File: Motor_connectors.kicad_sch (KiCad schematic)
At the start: 0 parts

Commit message: Motor connectors added check pinout with motor wiring
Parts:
- added UR1, UR2, UR3: 2367196-8, symbol 2367196-8:2367196-8
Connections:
- new net GND: UR1.4, UR1.MP1, UR1.MP2, UR2.4, UR2.MP1, UR2.MP2, UR3.4, UR3.MP1, UR3.MP2
- new net MOT_POW: UR1.5, UR2.5, UR3.5
- new net U_1: UR1.3
- new net U_2: UR2.3
- new net U_3: UR3.3
- new net U_HP_1: UR1.8
- new net U_HP_2: UR2.8
- new net U_HP_3: UR3.8
- new net V_1: UR1.2
- new net V_2: UR2.2
- new net V_3: UR3.2
- new net V_HP_1: UR1.7
- new net V_HP_2: UR2.7
- new net V_HP_3: UR3.7
- new net W_1: UR1.1
- new net W_2: UR2.1
- new net W_3: UR3.1
- new net W_HP_1: UR1.6
- new net W_HP_2: UR2.6
- new net W_HP_3: UR3.6

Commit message: MCU interfaces are done! Check the Changes and Complete ERC modifications
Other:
- company: (none) -> Parikshit Student Satellite Team
- title: (none) -> AOCS BOARD
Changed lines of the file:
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@@
 (kicad_sch (version 20211123) (generator eeschema)
   (paper "A4")
+  (title_block
+    (title "AOCS BOARD")
+    (company "Parikshit Student Satellite Team")
+  )
   (junction (at 133.35 55.88) (diameter 0) (color 0 0 0 0)
   )
@@
   )
   (wire (pts (xy 66.04 121.92) (xy 69.85 121.92))
+    (stroke (width 0) (type default) (color 0 0 0 0))
+  )
+  (wire (pts (xy 26.67 167.64) (xy 26.67 166.37))
     (stroke (width 0) (type default) (color 0 0 0 0))
   )
@@
   (symbol (lib_id "power:GND") (at 85.09 60.96 0) (unit 1)
     (in_bom yes) (on_board yes) (fields_autoplaced)
-    (property "Reference" "#PWR?" (id 0) (at 85.09 67.31 0)
+    (property "Reference" "#PWR0242" (id 0) (at 85.09 67.31 0)
       (effects (font (size 1.27 1.27)) hide)
     )
@@
   (symbol (lib_id "power:GND") (at 181.61 60.96 0) (unit 1)
     (in_bom yes) (on_board yes) (fields_autoplaced)
-    (property "Reference" "#PWR?" (id 0) (at 181.61 67.31 0)
+    (property "Reference" "#PWR0244" (id 0) (at 181.61 67.31 0)
       (effects (font (size 1.27 1.27)) hide)
     )
@@
   (symbol (lib_id "power:GND") (at 86.36 116.84 0) (unit 1)
     (in_bom yes) (on_board yes) (fields_autoplaced)
-    (property "Reference" "#PWR?" (id 0) (at 86.36 123.19 0)
+    (property "Reference" "#PWR0240" (id 0) (at 86.36 123.19 0)
       (effects (font (size 1.27 1.27)) hide)
     )
@@
   (symbol (lib_id "power:GND") (at 35.56 57.15 0) (unit 1)
     (in_bom yes) (on_board yes) (fields_autoplaced)
-    (property "Reference" "#PWR?" (id 0) (at 35.56 63.5 0)
+    (property "Reference" "#PWR0239" (id 0) (at 35.56 63.5 0)
       (effects (font (size 1.27 1.27)) hide)
     )
@@
     )
     (property "Datasheet" "" (id 3) (at 35.56 57.15 0)
+      (effects (font (size 1.27 1.27)) hide)
+    )
+    (pin "1")
+  )
+  (symbol (lib_id "power:GND") (at 26.67 167.64 0) (unit 1)
+    (in_bom yes) (on_board yes) (fields_autoplaced)
+    (property "Reference" "#PWR0275" (id 0) (at 26.67 173.99 0)
+      (effects (font (size 1.27 1.27)) hide)
+    )
+    (property "Value" "GND" (id 1) (at 26.67 172.085 0))
+    (property "Footprint" "" (id 2) (at 26.67 167.64 0)
+      (effects (font (size 1.27 1.27)) hide)
+    )
+    (property "Datasheet" "" (id 3) (at 26.67 167.64 0)
       (effects (font (size 1.27 1.27)) hide)
     )
@@
   (symbol (lib_id "power:GND") (at 38.1 114.3 0) (unit 1)
     (in_bom yes) (on_board yes) (fields_autoplaced)
-    (property "Reference" "#PWR?" (id 0) (at 38.1 120.65 0)
+    (property "Reference" "#PWR0241" (id 0) (at 38.1 120.65 0)
       (effects (font (size 1.27 1.27)) hide)
     )
@@
   (symbol (lib_id "power:GND") (at 133.35 58.42 0) (unit 1)
     (in_bom yes) (on_board yes) (fields_autoplaced)
-    (property "Reference" "#PWR?" (id 0) (at 133.35 64.77 0)
+    (property "Reference" "#PWR0243" (id 0) (at 133.35 64.77 0)
       (effects (font (size 1.27 1.27)) hide)
     )
@@
       (effects (font (size 1.27 1.27)) hide)
     )
+    (pin "1")
+  )
+  (symbol (lib_id "power:PWR_FLAG") (at 26.67 166.37 0) (unit 1)
+    (in_bom yes) (on_board yes) (fields_autoplaced)
+    (property "Reference" "#FLG0111" (id 0) (at 26.67 164.465 0)
+      (effects (font (size 1.27 1.27)) hide)
+    )
+    (property "Value" "PWR_FLAG" (id 1) (at 26.67 160.655 0))
+    (property "Footprint" "" (id 2) (at 26.67 166.37 0)
+      (effects (font (size 1.27 1.27)) hide)
+    )
+    (property "Datasheet" "~" (id 3) (at 26.67 166.37 0)
+      (effects (font (size 1.27 1.27)) hide)
+    )

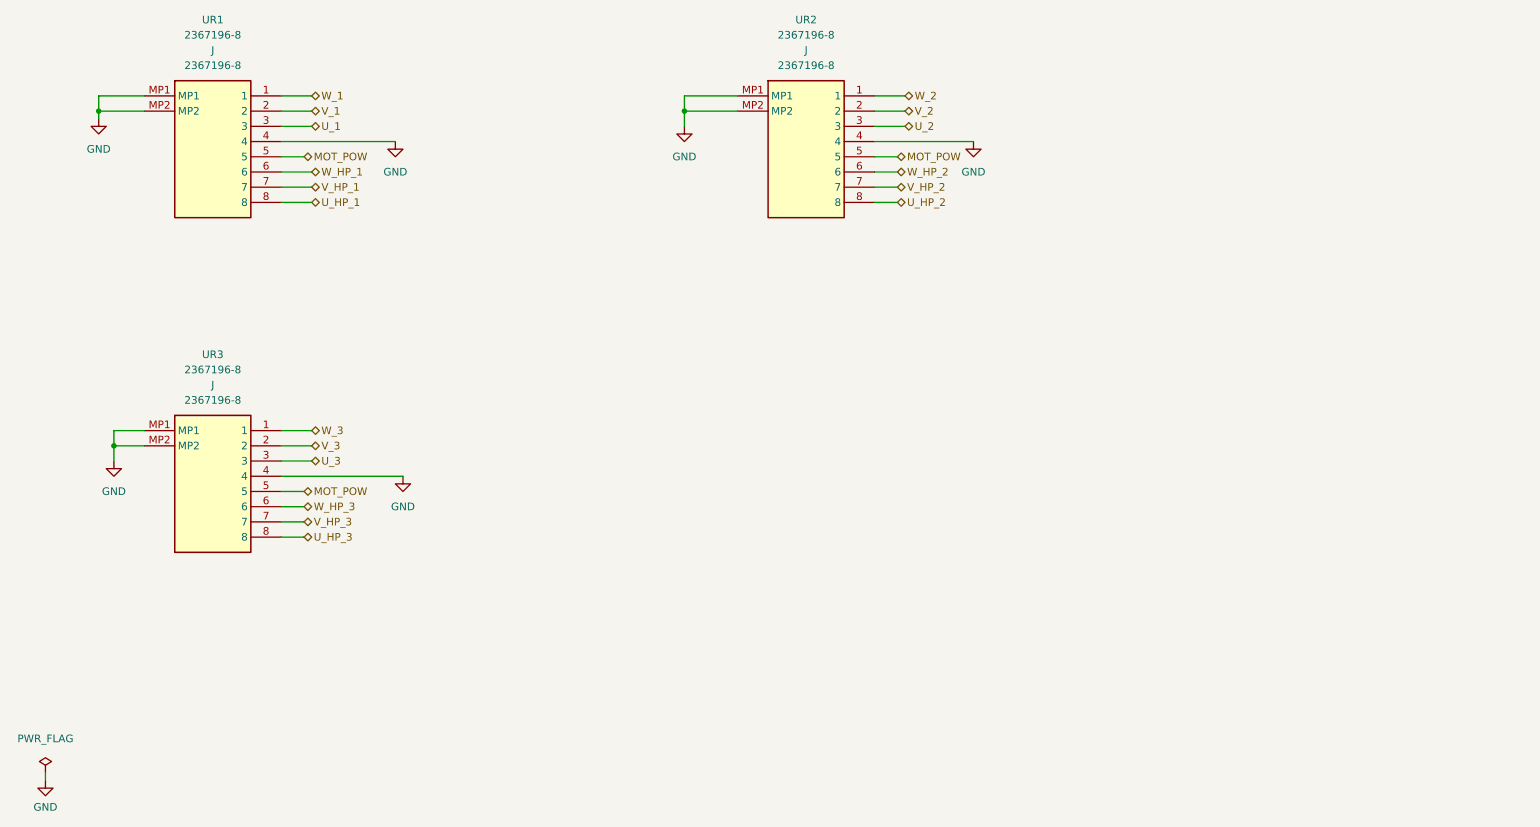
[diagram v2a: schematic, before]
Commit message: Max ERC errors corrected
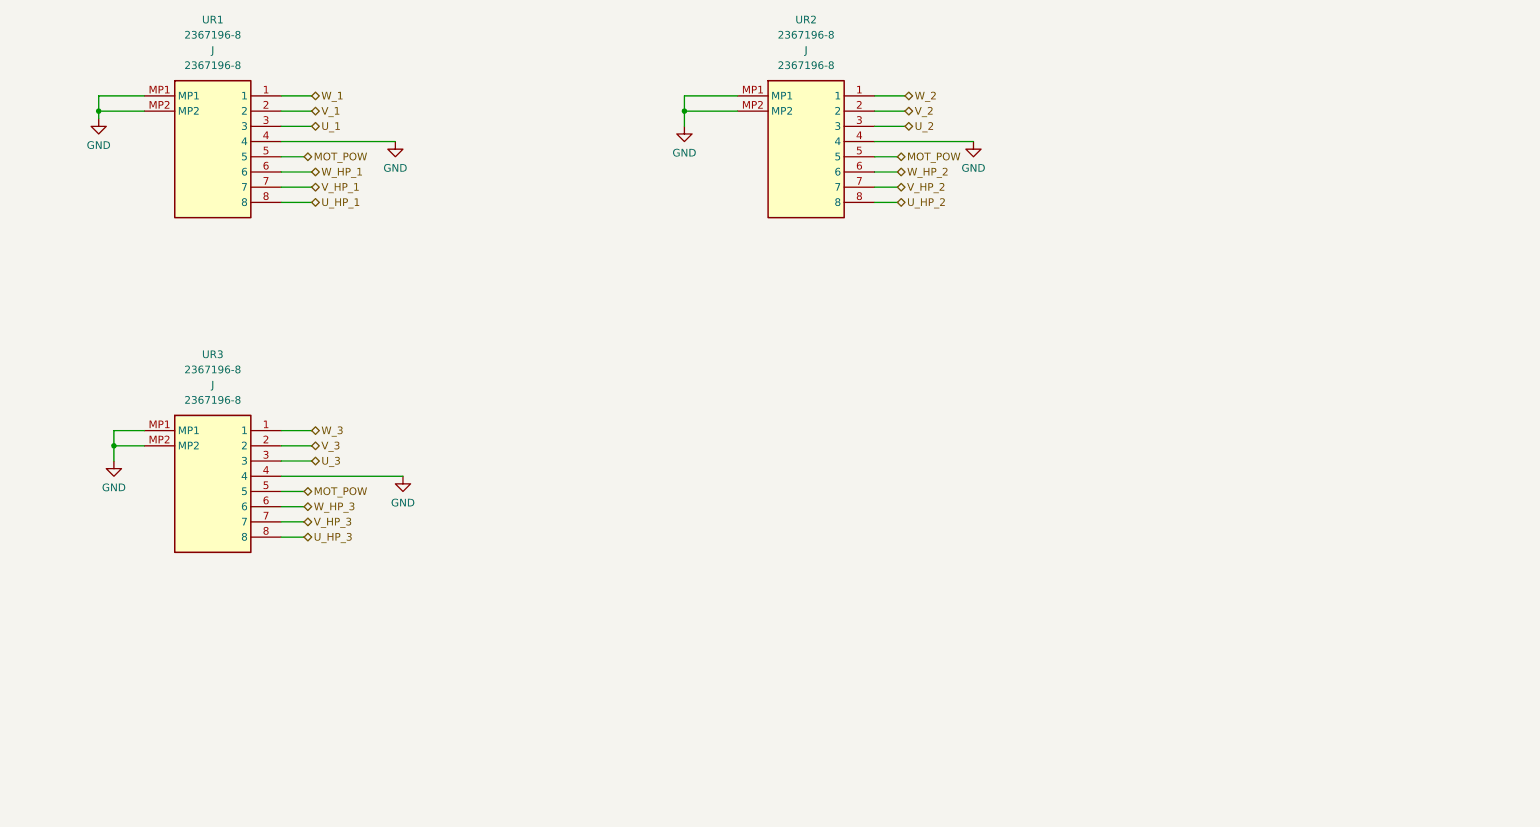
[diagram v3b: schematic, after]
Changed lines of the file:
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@@
-    (stroke (width 0) (type default) (color 0 0 0 0))
-  )
-  (wire (pts (xy 26.67 167.64) (xy 26.67 166.37))
     (stroke (width 0) (type default) (color 0 0 0 0))
   )
@@
     (pin "MP2")
   )
-  (symbol (lib_id "power:GND") (at 85.09 60.96 0) (unit 1)
-    (in_bom yes) (on_board yes) (fields_autoplaced)
-    (property "Reference" "#PWR0242" (id 0) (at 85.09 67.31 0)
-      (effects (font (size 1.27 1.27)) hide)
-    )
-    (property "Value" "GND" (id 1) (at 85.09 66.04 0))
-    (property "Footprint" "" (id 2) (at 85.09 60.96 0)
-      (effects (font (size 1.27 1.27)) hide)
-    )
-    (property "Datasheet" "" (id 3) (at 85.09 60.96 0)
-      (effects (font (size 1.27 1.27)) hide)
-    )
-    (pin "1")
-  )
-  (symbol (lib_id "power:GND") (at 181.61 60.96 0) (unit 1)
+  (symbol (lib_id "upsat-comms-hardware:GND") (at 133.35 58.42 0) (unit 1)
+    (in_bom yes) (on_board yes) (fields_autoplaced)
+    (property "Reference" "#PWR0243" (id 0) (at 133.35 64.77 0)
+      (effects (font (size 1.27 1.27)) hide)
+    )
+    (property "Value" "GND" (id 1) (at 133.35 62.865 0))
+    (property "Footprint" "" (id 2) (at 133.35 58.42 0))
+    (property "Datasheet" "" (id 3) (at 133.35 58.42 0))
+    (pin "1")
+  )
+  (symbol (lib_id "upsat-comms-hardware:GND") (at 85.09 60.96 0) (unit 1)
+    (in_bom yes) (on_board yes) (fields_autoplaced)
+    (property "Reference" "#PWR0239" (id 0) (at 85.09 67.31 0)
+      (effects (font (size 1.27 1.27)) hide)
+    )
+    (property "Value" "GND" (id 1) (at 85.09 65.405 0))
+    (property "Footprint" "" (id 2) (at 85.09 60.96 0))
+    (property "Datasheet" "" (id 3) (at 85.09 60.96 0))
+    (pin "1")
+  )
+  (symbol (lib_id "upsat-comms-hardware:GND") (at 181.61 60.96 0) (unit 1)
     (in_bom yes) (on_board yes) (fields_autoplaced)
     (property "Reference" "#PWR0244" (id 0) (at 181.61 67.31 0)
       (effects (font (size 1.27 1.27)) hide)
     )
-    (property "Value" "GND" (id 1) (at 181.61 66.04 0))
-    (property "Footprint" "" (id 2) (at 181.61 60.96 0)
-      (effects (font (size 1.27 1.27)) hide)
-    )
-    (property "Datasheet" "" (id 3) (at 181.61 60.96 0)
-      (effects (font (size 1.27 1.27)) hide)
-    )
-    (pin "1")
-  )
-  (symbol (lib_id "power:GND") (at 86.36 116.84 0) (unit 1)
-    (in_bom yes) (on_board yes) (fields_autoplaced)
-    (property "Reference" "#PWR0240" (id 0) (at 86.36 123.19 0)
-      (effects (font (size 1.27 1.27)) hide)
-    )
-    (property "Value" "GND" (id 1) (at 86.36 121.92 0))
-    (property "Footprint" "" (id 2) (at 86.36 116.84 0)
-      (effects (font (size 1.27 1.27)) hide)
-    )
-    (property "Datasheet" "" (id 3) (at 86.36 116.84 0)
-      (effects (font (size 1.27 1.27)) hide)
-    )
-    (pin "1")
-  )
-  (symbol (lib_id "power:GND") (at 35.56 57.15 0) (unit 1)
-    (in_bom yes) (on_board yes) (fields_autoplaced)
-    (property "Reference" "#PWR0239" (id 0) (at 35.56 63.5 0)
-      (effects (font (size 1.27 1.27)) hide)
-    )
-    (property "Value" "GND" (id 1) (at 35.56 62.23 0))
-    (property "Footprint" "" (id 2) (at 35.56 57.15 0)
-      (effects (font (size 1.27 1.27)) hide)
-    )
-    (property "Datasheet" "" (id 3) (at 35.56 57.15 0)
-      (effects (font (size 1.27 1.27)) hide)
-    )
-    (pin "1")
-  )
-  (symbol (lib_id "power:GND") (at 26.67 167.64 0) (unit 1)
-    (in_bom yes) (on_board yes) (fields_autoplaced)
-    (property "Reference" "#PWR0275" (id 0) (at 26.67 173.99 0)
-      (effects (font (size 1.27 1.27)) hide)
-    )
-    (property "Value" "GND" (id 1) (at 26.67 172.085 0))
-    (property "Footprint" "" (id 2) (at 26.67 167.64 0)
-      (effects (font (size 1.27 1.27)) hide)
-    )
-    (property "Datasheet" "" (id 3) (at 26.67 167.64 0)
-      (effects (font (size 1.27 1.27)) hide)
-    )
+    (property "Value" "GND" (id 1) (at 181.61 65.405 0))
+    (property "Footprint" "" (id 2) (at 181.61 60.96 0))
+    (property "Datasheet" "" (id 3) (at 181.61 60.96 0))
+    (pin "1")
+  )
+  (symbol (lib_id "upsat-comms-hardware:GND") (at 35.56 57.15 0) (unit 1)
+    (in_bom yes) (on_board yes) (fields_autoplaced)
+    (property "Reference" "#PWR0240" (id 0) (at 35.56 63.5 0)
+      (effects (font (size 1.27 1.27)) hide)
+    )
+    (property "Value" "GND" (id 1) (at 35.56 61.595 0))
+    (property "Footprint" "" (id 2) (at 35.56 57.15 0))
+    (property "Datasheet" "" (id 3) (at 35.56 57.15 0))
     (pin "1")
   )
@@
     (pin "MP2")
   )
-  (symbol (lib_id "power:GND") (at 38.1 114.3 0) (unit 1)
-    (in_bom yes) (on_board yes) (fields_autoplaced)
-    (property "Reference" "#PWR0241" (id 0) (at 38.1 120.65 0)
-      (effects (font (size 1.27 1.27)) hide)
-    )
-    (property "Value" "GND" (id 1) (at 38.1 119.38 0))
-    (property "Footprint" "" (id 2) (at 38.1 114.3 0)
-      (effects (font (size 1.27 1.27)) hide)
-    )
-    (property "Datasheet" "" (id 3) (at 38.1 114.3 0)
-      (effects (font (size 1.27 1.27)) hide)
-    )
-    (pin "1")
-  )
-  (symbol (lib_id "power:GND") (at 133.35 58.42 0) (unit 1)
-    (in_bom yes) (on_board yes) (fields_autoplaced)
-    (property "Reference" "#PWR0243" (id 0) (at 133.35 64.77 0)
-      (effects (font (size 1.27 1.27)) hide)
-    )
-    (property "Value" "GND" (id 1) (at 133.35 63.5 0))
-    (property "Footprint" "" (id 2) (at 133.35 58.42 0)
-      (effects (font (size 1.27 1.27)) hide)
-    )
-    (property "Datasheet" "" (id 3) (at 133.35 58.42 0)
-      (effects (font (size 1.27 1.27)) hide)
-    )
-    (pin "1")
-  )
-  (symbol (lib_id "power:PWR_FLAG") (at 26.67 166.37 0) (unit 1)
-    (in_bom yes) (on_board yes) (fields_autoplaced)
-    (property "Reference" "#FLG0111" (id 0) (at 26.67 164.465 0)
-      (effects (font (size 1.27 1.27)) hide)
-    )
-    (property "Value" "PWR_FLAG" (id 1) (at 26.67 160.655 0))
-    (property "Footprint" "" (id 2) (at 26.67 166.37 0)
-      (effects (font (size 1.27 1.27)) hide)
-    )
-    (property "Datasheet" "~" (id 3) (at 26.67 166.37 0)
-      (effects (font (size 1.27 1.27)) hide)
-    )
+  (symbol (lib_id "upsat-comms-hardware:GND") (at 86.36 116.84 0) (unit 1)
+    (in_bom yes) (on_board yes) (fields_autoplaced)
+    (property "Reference" "#PWR0241" (id 0) (at 86.36 123.19 0)
+      (effects (font (size 1.27 1.27)) hide)
+    )
+    (property "Value" "GND" (id 1) (at 86.36 121.285 0))
+    (property "Footprint" "" (id 2) (at 86.36 116.84 0))
+    (property "Datasheet" "" (id 3) (at 86.36 116.84 0))
     (pin "1")
   )
@@
     (pin "MP2")
   )
+  (symbol (lib_id "upsat-comms-hardware:GND") (at 38.1 114.3 0) (unit 1)
+    (in_bom yes) (on_board yes) (fields_autoplaced)
+    (property "Reference" "#PWR0242" (id 0) (at 38.1 120.65 0)
+      (effects (font (size 1.27 1.27)) hide)
+    )
+    (property "Value" "GND" (id 1) (at 38.1 118.745 0))
+    (property "Footprint" "" (id 2) (at 38.1 114.3 0))
+    (property "Datasheet" "" (id 3) (at 38.1 114.3 0))
+    (pin "1")
+  )
 )

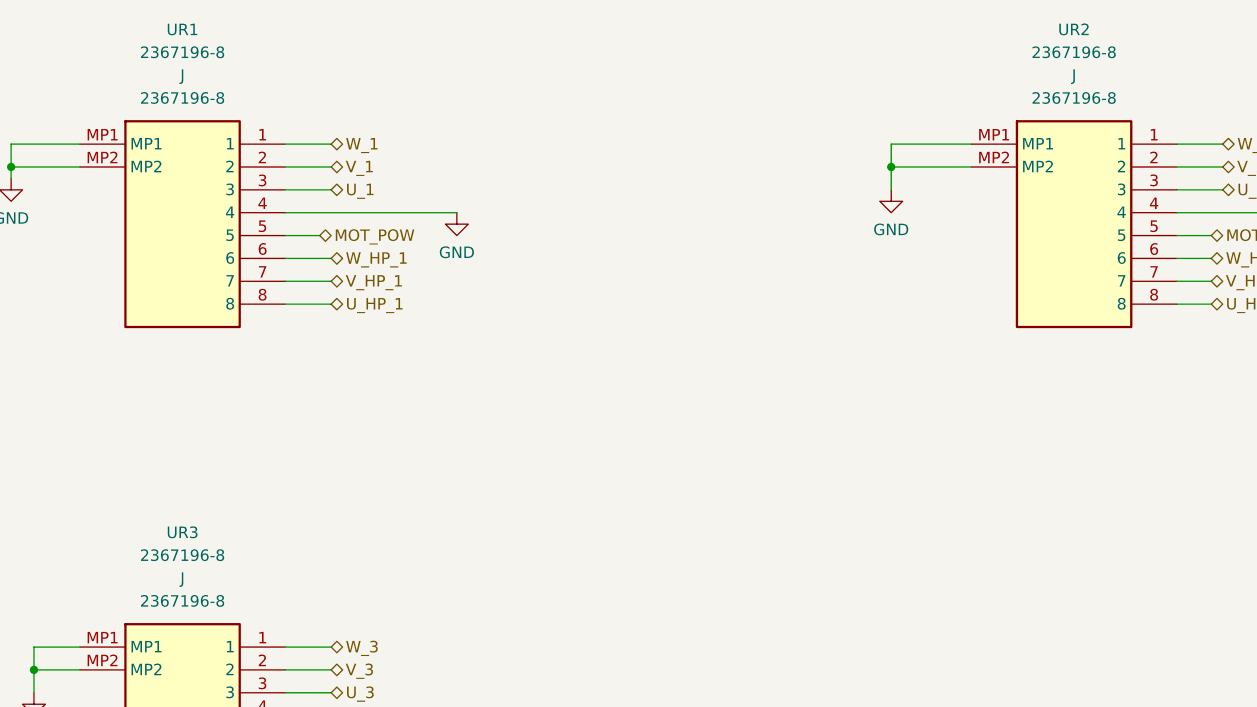
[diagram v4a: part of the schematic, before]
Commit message: Placed NCs at ADCS_HMC1051
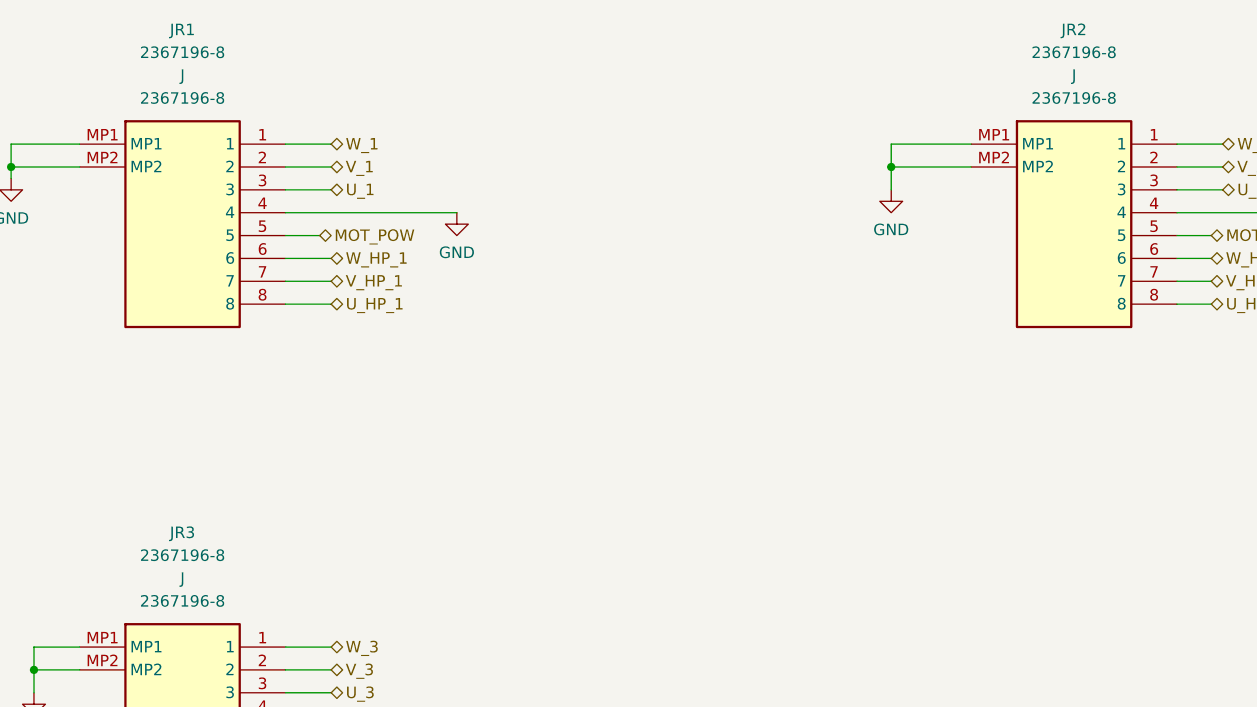
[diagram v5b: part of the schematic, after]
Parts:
- renumbered UR1 to JR1, UR2 to JR2, UR3 to JR3
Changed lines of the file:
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@@
   (symbol (lib_id "2367196-8:2367196-8") (at 43.18 53.34 0) (unit 1)
     (in_bom yes) (on_board yes) (fields_autoplaced)
-    (property "Reference" "UR1" (id 0) (at 54.61 40.64 0))
+    (property "Reference" "JR1" (id 0) (at 54.61 40.64 0))
     (property "Value" "2367196-8" (id 1) (at 54.61 43.18 0))
     (property "Footprint" "" (id 2) (at 43.18 53.34 0)
@@
   (symbol (lib_id "2367196-8:2367196-8") (at 43.18 109.22 0) (unit 1)
     (in_bom yes) (on_board yes) (fields_autoplaced)
-    (property "Reference" "UR3" (id 0) (at 54.61 96.52 0))
+    (property "Reference" "JR3" (id 0) (at 54.61 96.52 0))
     (property "Value" "2367196-8" (id 1) (at 54.61 99.06 0))
     (property "Footprint" "" (id 2) (at 43.18 109.22 0)
@@
   (symbol (lib_id "2367196-8:2367196-8") (at 142.24 53.34 0) (unit 1)
     (in_bom yes) (on_board yes) (fields_autoplaced)
-    (property "Reference" "UR2" (id 0) (at 153.67 40.64 0))
+    (property "Reference" "JR2" (id 0) (at 153.67 40.64 0))
     (property "Value" "2367196-8" (id 1) (at 153.67 43.18 0))
     (property "Footprint" "" (id 2) (at 142.24 53.34 0)
